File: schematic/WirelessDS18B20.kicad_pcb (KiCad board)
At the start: 2 copper layers, 26 x 33 mm, 13 parts, among them P1 Power Connector, P2 1-Wire Bus, P3 SERIAL_TX, Q1 BS170, SW1 RESCUE_MODE, SW2 RESET, U1 LM1117 3.3, U2 ESP-01

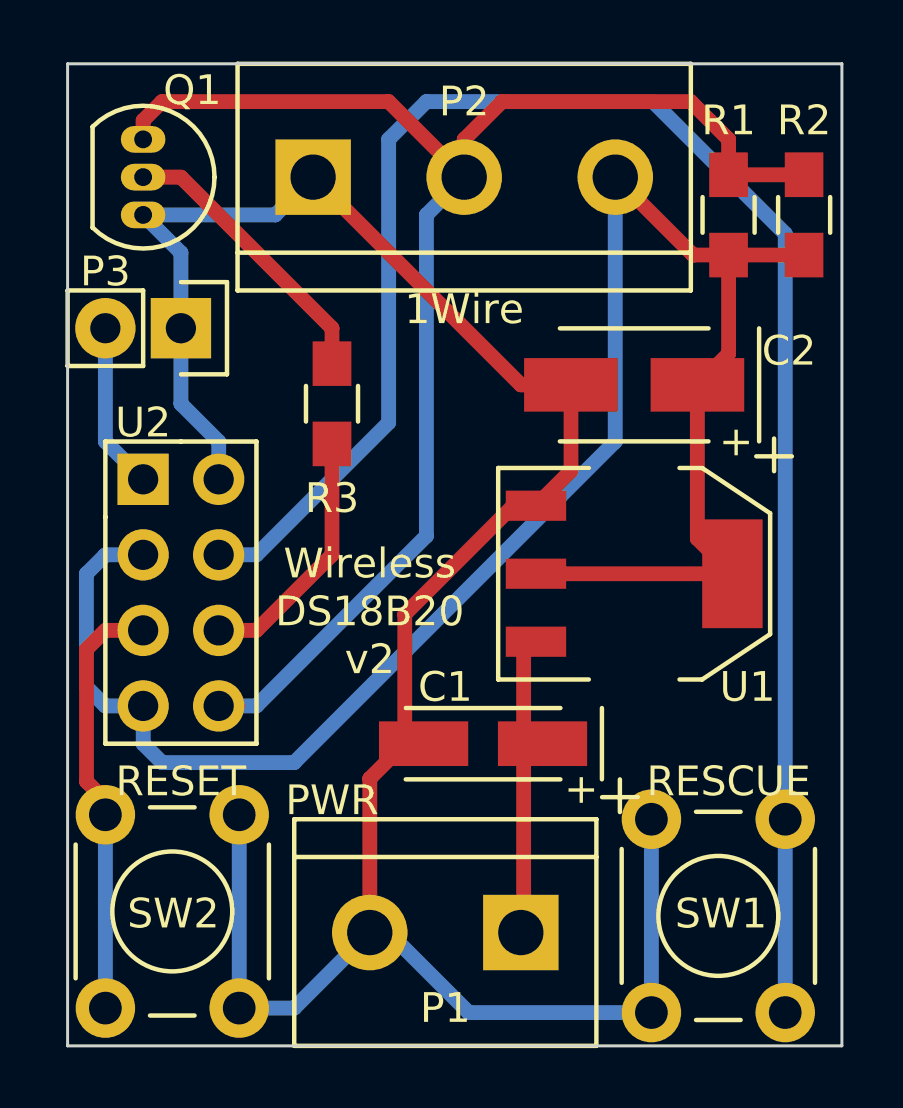
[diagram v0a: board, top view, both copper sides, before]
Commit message: Update Schematic
Addition of power diode against bad connection + reduce board size
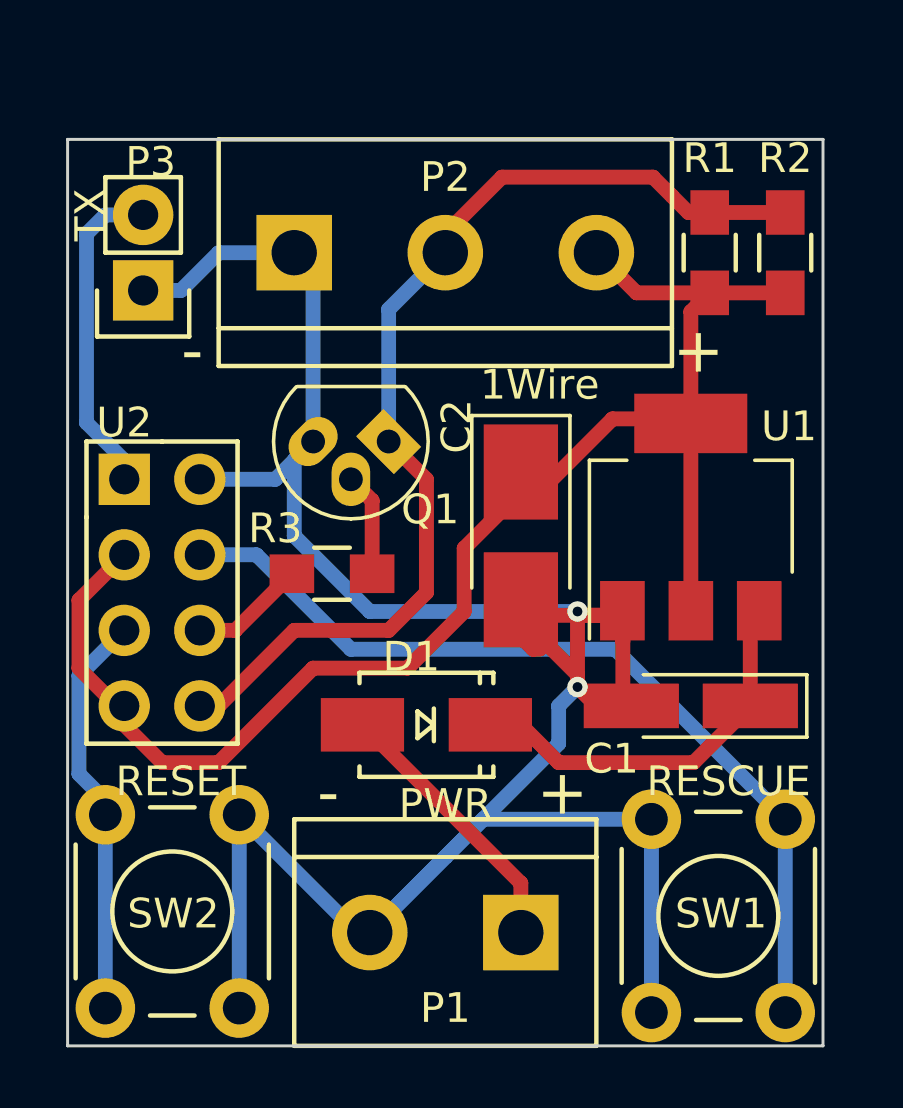
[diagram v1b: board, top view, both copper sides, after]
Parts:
- added D1: SS34, Diodes_SMD_Custom:SMA_Handsoldering_Custom, F.Cu at (130.8, 84.5)
- C1: footprint Capacitors_Tantalum_SMD:TantalC_SizeA_EIA-3216_HandSoldering -> Capacitors_Tantalum_SMD:CP_Tantalum_Case-A_EIA-3216-18_Hand
- C2: footprint Capacitors_Tantalum_SMD:TantalC_SizeB_EIA-3528_HandSoldering -> Capacitors_Tantalum_SMD:CP_Tantalum_Case-B_EIA-3528-21_Hand
- Q1: footprint TO_SOT_Packages_THT:TO-92_Inline_Narrow_Oval -> TO_SOT_Packages_THT:TO-92_Molded_Narrow_Oval
- U1: value LM1117 3.3 -> AMS1117 3.3
- moved Q1 13.1 mm to (129.5, 74.9), turned to 180 degrees
- moved C1 7.10 mm to (139.7, 83.8)
- moved C2 6.35 mm to (134.0, 78.1), turned to 270 degrees
- moved R3 5.72 mm to (127.6, 79.4), turned to 0 degrees
- moved U1 2.69 mm to (139.7, 77.5), turned to 90 degrees
- moved P2 2.62 mm to (131.4, 68.6)
- moved P3 1.80 mm to (121.3, 69.8), turned to 180 degrees
- moved R1 1.42 mm to (140.3, 68.6)
- moved R2 1.42 mm to (142.9, 68.6)
- moved U2 0.63 mm to (120.7, 76.2)
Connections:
- P1 pad 1: Net-(C1-Pad1) -> Net-(D1-Pad2)
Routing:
- net Net-(SW1-Pad1): track 59.0 -> 29.9 mm
- net Net-(P2-Pad2): track 50.3 -> 35.3 mm
- net VCC: track 64.6 -> 51.0 mm
- net GND: track 79.1 -> 91.3 mm, vias 0 -> 2
- net Net-(D1-Pad2): track 0.00 -> 9.19 mm
- net Net-(Q1-Pad2): track 9.64 -> 3.47 mm
- net Net-(P3-Pad2): track 5.61 -> 10.9 mm
- net Net-(R3-Pad1): track 8.59 -> 3.88 mm
- net Net-(C1-Pad1): track 9.99 -> 13.6 mm
- net Net-(SW2-Pad1): track 14.5 -> 13.7 mm
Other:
- board size 26 x 33 mm -> 25.4 x 30.5 mm
- net class Default: clearance 0.3 -> 0.2
- rule trace_clearance: 0.3 -> 0.2
- board text added: "+"
- board text added: "-"
- board text added: "TX"
- board text added: "V1.2"
- board text added: "Wireless DS18B20"
- board text removed: "Wireless DS18B20 v2"
